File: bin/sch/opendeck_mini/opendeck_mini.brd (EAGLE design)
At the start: 87 x 62 mm, 137 parts, among them Q1 BSS314PEH6327XTSA1, Q2 NTGD3148N, Q5 NTGD3148N, U1 6N137, U2 AT90USB1286, U3 MC14067BDWR2G-SO24W, U4 74HC165, U5 74HC165, Y1 16MHz

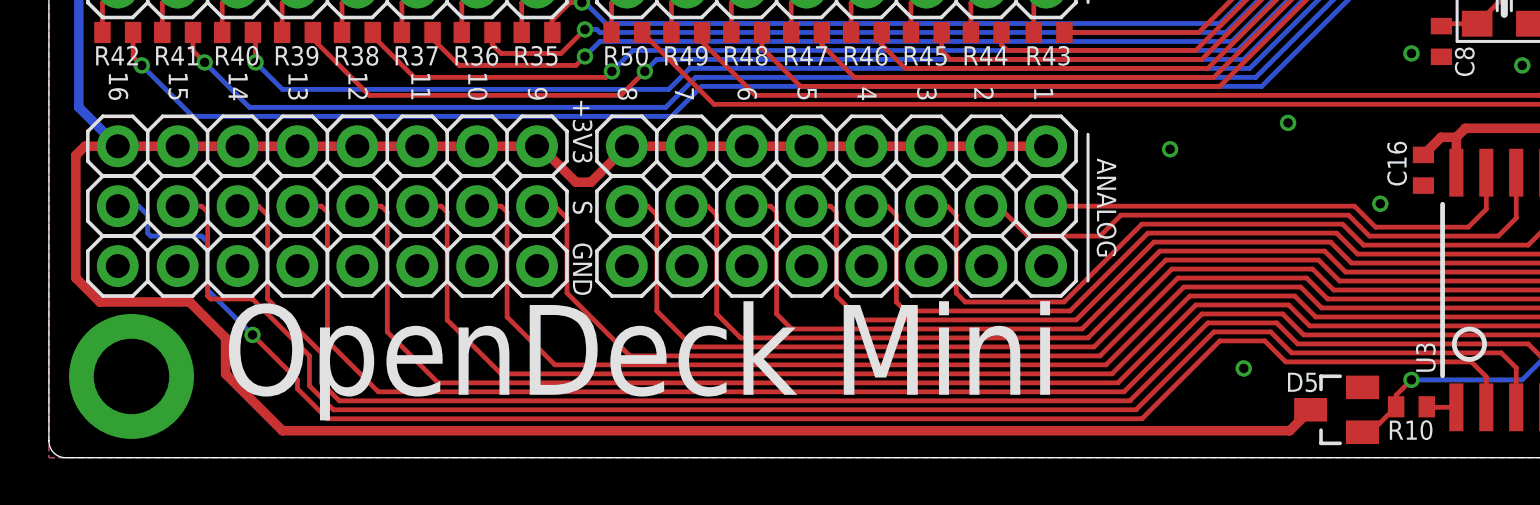
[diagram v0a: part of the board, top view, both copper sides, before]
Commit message: targets/opendeck_mini: remove schottky diode on adc input
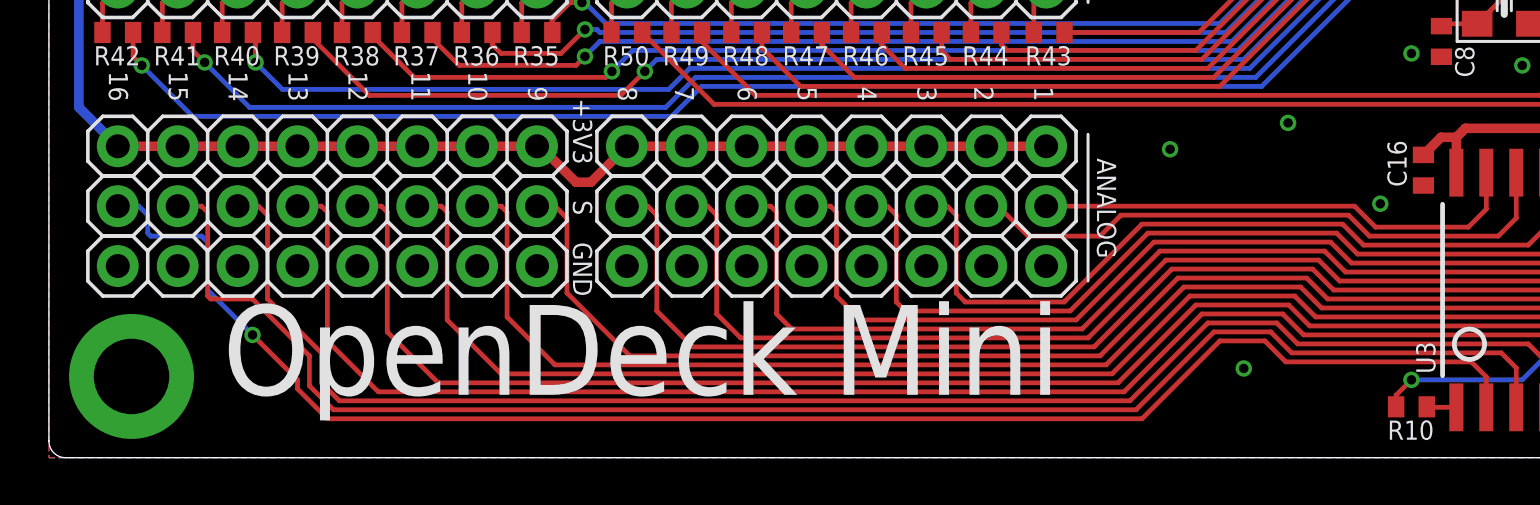
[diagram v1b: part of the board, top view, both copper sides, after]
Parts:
- removed D5: BAT46-SOT23, igor_lbr:SOT23
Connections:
- net +3V3: no longer D5.3
- net N$20: no longer D5.1
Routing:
- net +3V3: track 199.0 -> 135.5 mm
- net N$20: track 61.5 -> 59.6 mm
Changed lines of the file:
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@@
 <attribute name="NAME" x="70.485" y="37.846" size="0.8128" layer="25" font="vector" ratio="15"/>
-</element>
-<element name="D5" library="igor_lbr" package="SOT23" value="BAT46-SOT23" x="54.61" y="2.032" smashed="yes" rot="R180">
-<attribute name="NAME" x="52.451" y="2.794" size="0.8128" layer="25" font="vector" ratio="15"/>
-<attribute name="MANUFACTURER" value="Micro Commercial Components (MCC)" x="54.61" y="2.032" size="1.778" layer="27" rot="R180" display="off"/>
-<attribute name="MPN" value="MMBD301-TP" x="54.61" y="2.032" size="1.778" layer="27" rot="R180" display="off"/>
 </element>
 <element name="D6" library="igor_lbr" package="0805_LED" value="Green" x="82.677" y="51.435" smashed="yes">
@@
 <contactref element="CONN7" pad="2"/>
 <contactref element="CONN7" pad="1"/>
-<contactref element="D5" pad="3"/>
 <wire x1="56.291" y1="40.102" x2="56.941" y2="39.452" width="0.4064" layer="1"/>
 <wire x1="56.941" y1="38.788" x2="56.941" y2="39.452" width="0.4064" layer="1"/>
@@
 <wire x1="48.641" y1="39.116" x2="46.228" y2="39.116" width="0.4064" layer="1"/>
 <wire x1="45.72" y1="39.624" x2="45.72" y2="40.552" width="0.4064" layer="1"/>
-<wire x1="2.921" y1="13.208" x2="1.524" y2="13.208" width="0.4064" layer="1"/>
-<wire x1="1.143" y1="12.827" x2="1.143" y2="7.62" width="0.4064" layer="1"/>
-<wire x1="1.143" y1="7.62" x2="2.159" y2="6.604" width="0.4064" layer="1"/>
 <wire x1="20.701" y1="13.208" x2="20.828" y2="13.208" width="0.4064" layer="1"/>
 <wire x1="20.828" y1="13.208" x2="22.352" y2="11.684" width="0.4064" layer="1"/>
@@
 <wire x1="1.27" y1="33.02" x2="1.27" y2="14.859" width="0.4064" layer="16"/>
 <wire x1="1.27" y1="14.859" x2="2.921" y2="13.208" width="0.4064" layer="16"/>
-<wire x1="1.524" y1="13.208" x2="1.143" y2="12.827" width="0.4064" layer="1"/>
 <wire x1="6.858" y1="44.196" x2="6.477" y2="43.815" width="0.4064" layer="1"/>
 <wire x1="6.477" y1="43.815" x2="6.477" y2="41.529" width="0.4064" layer="1"/>
 <wire x1="2.921" y1="13.208" x2="5.461" y2="13.208" width="0.4064" layer="1"/>
-<wire x1="2.159" y1="6.604" x2="5.969" y2="6.604" width="0.4064" layer="1"/>
-<wire x1="9.906" y1="1.143" x2="52.621" y2="1.143" width="0.4064" layer="1"/>
-<wire x1="5.969" y1="6.604" x2="7.493" y2="5.08" width="0.4064" layer="1"/>
-<wire x1="7.493" y1="5.08" x2="7.493" y2="3.556" width="0.4064" layer="1"/>
-<wire x1="7.493" y1="3.556" x2="9.906" y2="1.143" width="0.4064" layer="1"/>
 <wire x1="56.291" y1="40.102" x2="49.083" y2="40.102" width="0.4064" layer="1"/>
 <wire x1="49.083" y1="40.102" x2="48.829" y2="40.356" width="0.4064" layer="1"/>
-<wire x1="52.621" y1="1.143" x2="53.51" y2="2.032" width="0.4064" layer="1"/>
 </signal>
 <signal name="MISO">
@@
 <signal name="N$20">
 <contactref element="U2" pad="61"/>
-<contactref element="D5" pad="1"/>
 <contactref element="R10" pad="1"/>
 <wire x1="57.135" y1="2.159" x2="57.135" y2="2.652" width="0.2032" layer="1"/>
@@
 <wire x1="65.278" y1="20.447" x2="65.278" y2="6.096" width="0.2032" layer="16"/>
 <wire x1="65.278" y1="6.096" x2="62.484" y2="3.302" width="0.2032" layer="16"/>
-<wire x1="55.71" y1="1.082" x2="56.058" y2="1.082" width="0.2032" layer="1"/>
-<wire x1="56.058" y1="1.082" x2="57.135" y2="2.159" width="0.2032" layer="1"/>
 </signal>
 <signal name="BTLDR_SW">
